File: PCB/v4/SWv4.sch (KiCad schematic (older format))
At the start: 5 parts

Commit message: start v4 schem
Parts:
- added C? (x2): 1uF, symbol C
- added C?: 10uF/16V, symbol C
- added J?: LRA, symbol CONN_01X02
- added R?: 920K, symbol R
- added R? (x4): 10K, symbol R
- added SW?: BTN_TL, symbol SW_Push_45deg
- added SW?: BTN_BL, symbol SW_Push_45deg
- added SW?: BTN_BR, symbol SW_Push_45deg
- added SW?: BTN_TR, symbol SW_Push_45deg
- added U?: CP2102, symbol CP2102
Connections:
- net labels added: +12V, +3V3, +BATT, CS(OLED), D/C, GND, MOSI, RST(OLED), SCLK
- wire segments 0 -> 33
- no-connect marks 0 -> 1
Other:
- moved on the sheet: U?, X?

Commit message: update v4 schem & create v4 sheets
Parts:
- removed J?: Micro_SD_Card, symbol Micro_SD_Card
- removed R? (x3): 10K, symbol R
- removed SW?: BTN_BL, symbol SW_Push_45deg
- removed SW?: BTN_BR, symbol SW_Push_45deg
- removed SW?: BTN_TR, symbol SW_Push_45deg
- added C? (x3): 10uF, symbol C
- added C?: 0.1uF, symbol C
- added C?: 10uF/15V, symbol C
- added C?: 10uF/16V, symbol C
- added D?: BAT54T1G, symbol D_Schottky_Small
- added J?: Micro_SD_Card_SPI, symbol Micro_SD_Card_SPI
- added L?: 10uH, symbol L
- added R? (x4): 10K, symbol R
- added R?: 100K, symbol R
- added SW?: BTN_TR, symbol SW_Push_45deg
- added SW?: BTN_BL, symbol SW_Push_45deg
- added SW?: BTN_BR, symbol SW_Push_45deg
- added U?: FAN5331, symbol FAN5331
- J?: value USB_OTG -> microUSB
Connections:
- net labels added: +5V, BTN-BL, BTN-BR, BTN-TL, BTN-TR, CS(SD), D+, D-, MISO, RXD, SCL, SDA, TXD
- wire segments 33 -> 92
- no-connect marks 1 -> 17
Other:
- note added: "Buttons"
- note added: "Display Voltage Boost"
- note added: "Haptics"
- note added: "OLED Display\nInterface"
- note added: "SD Card (SPI) - SD Interface Compat. ?"
- note added: "USB interface (Serial / PWR)"
- moved on the sheet: C?, J?, R?, SW?, U?

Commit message: sync
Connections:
- net DRV_EN: now reaches U?.5 (EN)
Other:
- moved on the sheet: C?

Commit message: sync
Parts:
- removed R? (x4): 10K, symbol R
- removed SW?: BTN_TL, symbol SW_Push_45deg
- removed SW?: BTN_TR, symbol SW_Push_45deg
- removed SW?: BTN_BL, symbol SW_Push_45deg
- removed SW?: BTN_BR, symbol SW_Push_45deg
- added C? (x4): 1nF/50V, symbol C
- added Q? (x2): S8050(NPN), TO_SOT_Packages_THT:TO-92_Molded_Narrow, symbol S8050
- added R? (x4): 470R, symbol R
- added R? (x4): 5K, symbol R
- added R? (x2): 12K, symbol R
- added SW?: BTN_TL, symbol SW_Push_45deg
- added SW?: BTN_TR, symbol SW_Push_45deg
- added SW?: BTN_BL, symbol SW_Push_45deg
- added SW?: BTN_BR, symbol SW_Push_45deg
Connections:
- net +3V3: now also R?.1, R?.1, R?.1, R?.1
- net BTN-BL: now also R?.2, R?.2
- net BTN-BR: now also R?.2, R?.2
- net BTN-TL: now also R?.2, R?.2
- net BTN-TR: now also R?.2, R?.2
- net GND: now also U?.1 (GND), U?.15 (GND), U?.38 (GND), U?.39 (GND-PAD), C?.2, C?.2, C?.2, C?.2, SW?.2, SW?.2, SW?.2, SW?.2
- net RXD: no longer U?.25 (RXD)
- net TXD: no longer U?.26 (TXD)
- net IO0: now reaches U?.25 (IO0)
- net IO0: now also Q?.3 (C)
- net ESP_EN: now reaches U?.3 (EN)
- net ESP_EN: now also Q?.3 (C)
- net RTS: now reaches U?.24 (RTS)
- net RTS: now also Q?.1 (E), R?.2
- net DTR: now reaches U?.28 (DTR)
- net DTR: now also Q?.1 (E), R?.2
- new net: C?.1, R?.1, SW?.1 (x4)
- new net: Q?.2 (B), R?.1 (x2)
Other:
- note added: "Add BTN-?? here"
- note added: "Auto Reset"

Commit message: start adafruit rebase
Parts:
- removed U?: CP2102, symbol CP2102
- added C? (x4): 10uF, symbol C
- added C?: 1uF, symbol C
- added D?: LED, symbol LED
- added D?: D_Schottky, symbol D_Schottky
- added J?: BATT, symbol CONN_01X02
- added R?: 1K, symbol R
- added R?: ???K, symbol R
- added R? (x2): 100K, symbol R
- added U?: CP2104, symbol CP2104
- added U?: MCP73831/2, symbol MCP73831/2
- added U?: AP2112/3V3, symbol AP2112/3V3
- R? (x2): value 12K -> 10K
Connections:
- net +3V3: now also C?.1, C?.1, C?.1, U?.5 (OUT), U?.5 (VIO), U?.6 (VDD), U?.7 (REGIN)
- net +5V: now also D?.2 (A), D?.2 (A), R?.1, U?.4 (VDD), U?.8 (VBUS)
- net +BATT: now also C?.2, J?.1 (P1), U?.3 (VBAT)
- net D+: now also U?.3 (D+)
- net D-: now also U?.4 (D-)
- net DTR: now also U?.23 (DTR)
- net GND: now also C?.1, C?.2, C?.2, C?.2, C?.2, J?.2 (P2), R?.2, R?.2, U?.2 (GND), U?.2 (GND), U?.2 (VSS)
- net RTS: now also U?.19 (RTS)
- net RXD: now also U?.20 (RXD)
- net TXD: now also U?.21 (TXD)
- new net: D?.1 (K), R?.1
- new net: R?.2, U?.1 (STAT)
- new net: R?.1, U?.5 (PROG)
- new net: C?.1, D?.1 (K), R?.1, U?.1 (IN)
- new net: R?.2, U?.3 (EN)
- no-connect marks 17 -> 20
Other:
- note added: "LIPO Charge"
- note added: "Power / Filtering?"
- note added: "Ref Ada\n(Link GNDs?)"
- note added: "USB Interface"
- note removed: "USB interface (Serial / PWR)"
- moved on the sheet: Q?, R?

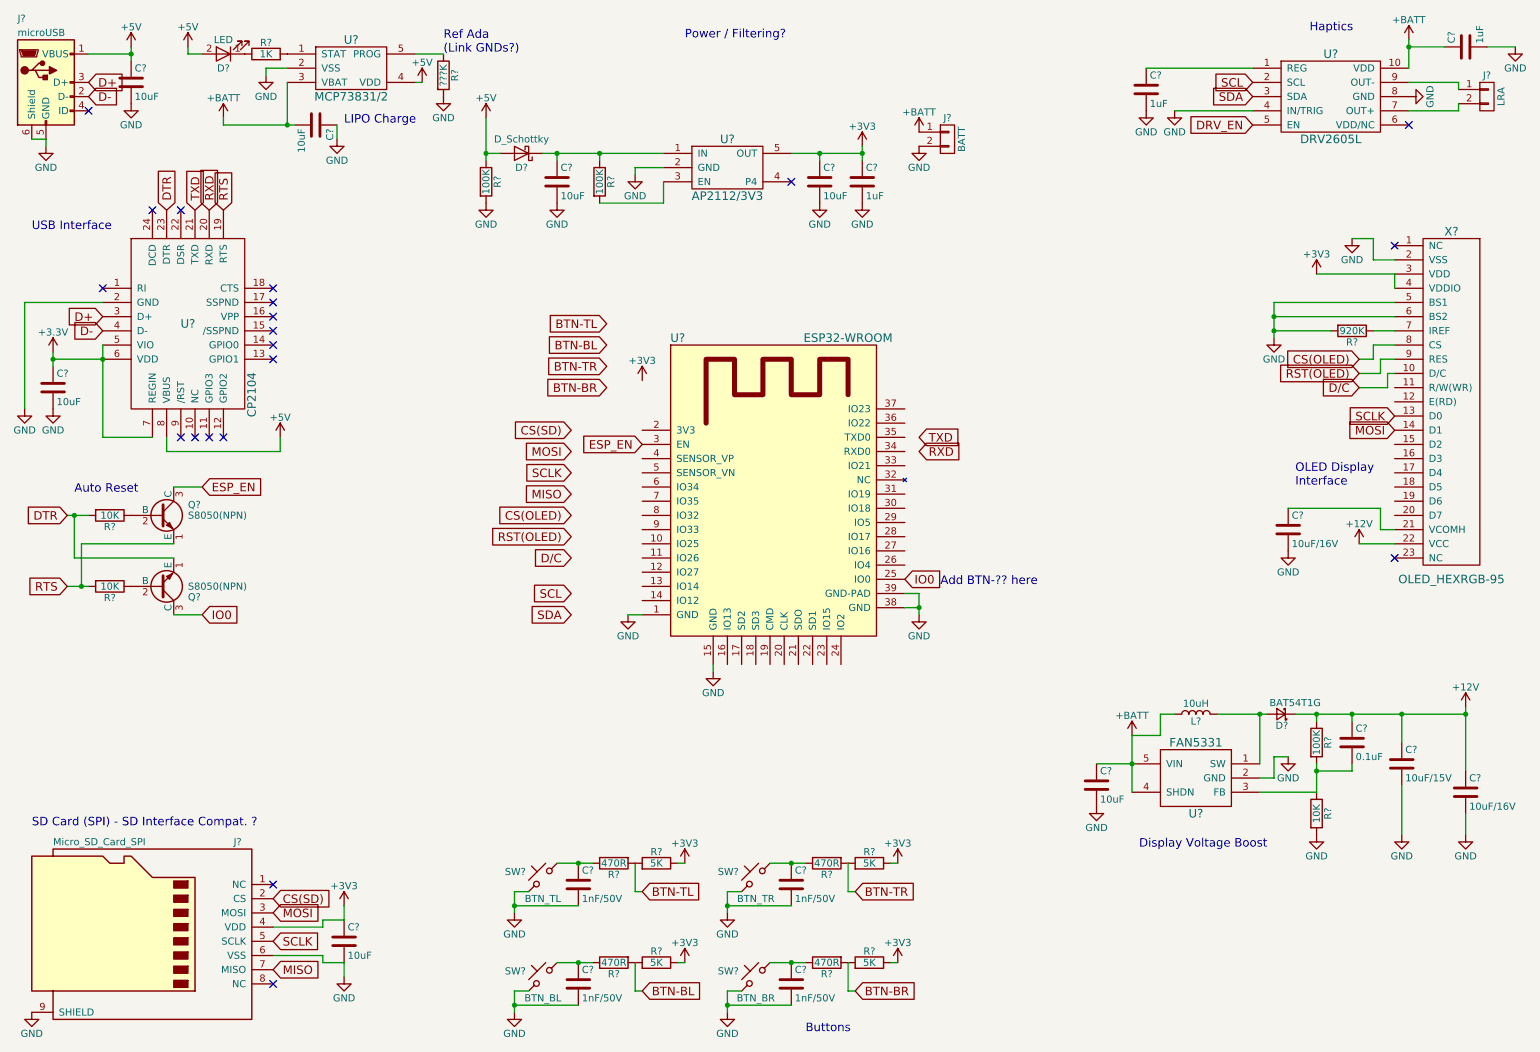
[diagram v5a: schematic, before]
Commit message: add feather ref & feather vbatt-lvl
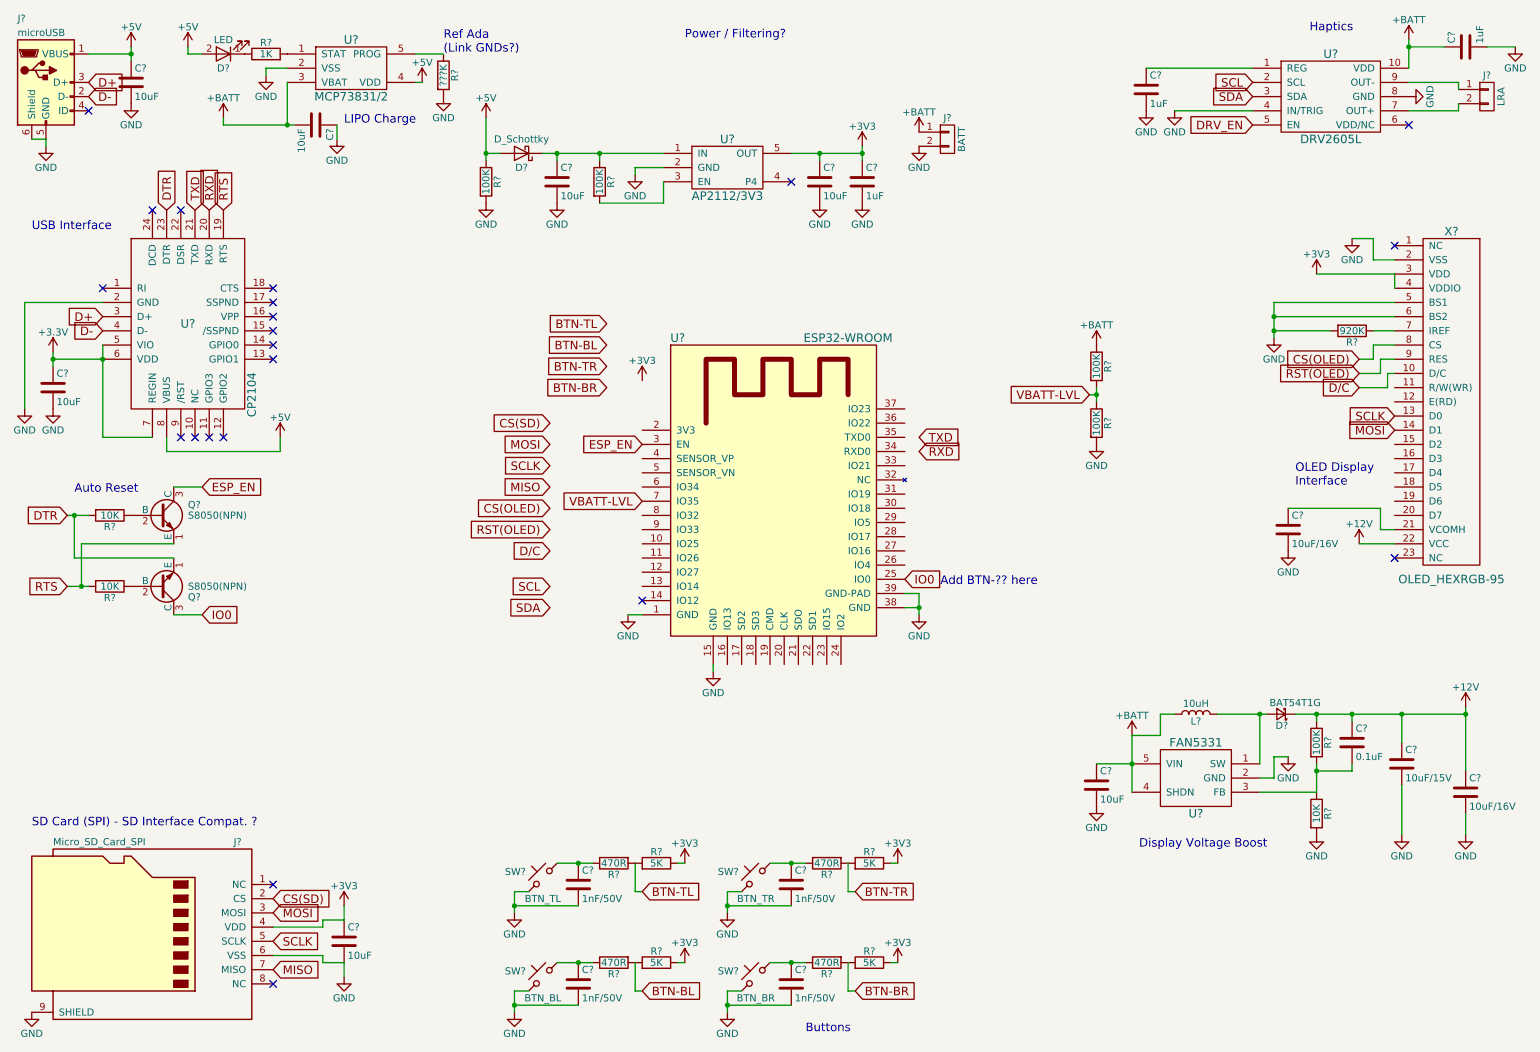
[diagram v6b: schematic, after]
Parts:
- added R? (x2): 100K, symbol R
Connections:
- net +BATT: now also R?.1
- net GND: now also R?.2
- net VBATT-LVL: now reaches U?.7 (IO35)
- net VBATT-LVL: now also R?.1, R?.2
- no-connect marks 20 -> 21
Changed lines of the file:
@@
 Text GLabel 4700 3150 0    60   Input ~ 0
 BTN-BR
-Text GLabel 4450 3450 0    60   Input ~ 0
+Text GLabel 4300 3400 0    60   Input ~ 0
 CS(SD)
-Text GLabel 4450 3600 0    60   Input ~ 0
+Text GLabel 4300 3550 0    60   Input ~ 0
 MOSI
-Text GLabel 4450 3750 0    60   Input ~ 0
+Text GLabel 4300 3700 0    60   Input ~ 0
 SCLK
-Text GLabel 4450 3900 0    60   Input ~ 0
+Text GLabel 4300 3850 0    60   Input ~ 0
 MISO
-Text GLabel 4450 4050 0    60   Input ~ 0
+Text GLabel 4300 4000 0    60   Input ~ 0
 CS(OLED)
-Text GLabel 4450 4200 0    60   Input ~ 0
+Text GLabel 4300 4150 0    60   Input ~ 0
 RST(OLED)
-Text GLabel 4450 4350 0    60   Input ~ 0
+Text GLabel 4300 4300 0    60   Input ~ 0
 D/C
-Text GLabel 4450 4600 0    60   Input ~ 0
+Text GLabel 4300 4550 0    60   Input ~ 0
 SCL
-Text GLabel 4450 4750 0    60   Input ~ 0
+Text GLabel 4300 4700 0    60   Input ~ 0
 SDA
 Text GLabel 1800 1900 1    60   Input ~ 0
@@
 	10700 1200 10700 1150
 Wire Wire Line
-	10350 700  10350 750
-Wire Wire Line
-	10350 750  10350 900
+	10350 700  10350 900
 Connection ~ 10350 750
 Wire Wire Line
@@
 	10250 2650 9400 2650
 Wire Wire Line
-	9400 2550 9400 2650
-Wire Wire Line
-	9400 2650 9400 2750
-Wire Wire Line
-	9400 2750 9400 2800
+	9400 2550 9400 2800
 Wire Wire Line
 	10250 2550 9400 2550
@@
 	1050 800  1350 800
 Wire Wire Line
-	1350 750  1350 800
-Wire Wire Line
-	1350 800  1350 850
+	1350 750  1350 850
 Connection ~ 1350 800
 Wire Wire Line
-	8400 5600 8400 5800
-Wire Wire Line
-	8400 5800 8400 6000
+	8400 5600 8400 6000
 Connection ~ 8400 5800
 Wire Wire Line
@@
 	9300 5800 9300 5450
 Wire Wire Line
-	9000 5450 9300 5450
-Wire Wire Line
-	9300 5450 9350 5450
+	9000 5450 9350 5450
 Connection ~ 9300 5450
 Wire Wire Line
@@
 	9700 6000 9300 6000
 Wire Wire Line
-	9550 5450 9700 5450
-Wire Wire Line
-	9700 5450 9950 5450
-Wire Wire Line
-	9950 5450 10300 5450
-Wire Wire Line
-	10300 5450 10750 5450
+	9550 5450 10750 5450
 Wire Wire Line
 	10300 5450 10300 5650
@@
 	10750 6300 10750 6150
 Wire Wire Line
-	10750 5400 10750 5450
-Wire Wire Line
-	10750 5450 10750 5850
+	10750 5400 10750 5850
 Connection ~ 10750 5450
 Connection ~ 10300 5450
@@
 Connection ~ 9950 5450
 Wire Wire Line
-	9700 5800 9700 5850
-Wire Wire Line
-	9700 5850 9700 6000
+	9700 5800 9700 6000
 Wire Wire Line
 	9700 5850 9950 5850
@@
 	6800 4600 6900 4600
 Wire Wire Line
-	6900 4600 6900 4700
-Wire Wire Line
-	6900 4700 6900 4750
+	6900 4600 6900 4750
 Wire Wire Line
 	6800 4700 6900 4700
@@
 	1650 4750 1850 4750
 Wire Wire Line
-	900  4050 950  4050
-Wire Wire Line
-	950  4050 1050 4050
-Wire Wire Line
-	900  4550 1000 4550
-Wire Wire Line
-	1000 4550 1050 4550
+	900  4050 1050 4050
+Wire Wire Line
+	900  4550 1050 4550
 Wire Wire Line
 	950  4350 1650 4350
@@
 	4050 6700 4150 6700
 Wire Wire Line
-	4050 6700 4050 6800
-Wire Wire Line
-	4050 6800 4050 6850
+	4050 6700 4050 6850
 Wire Wire Line
 	4050 6800 4500 6800
 Connection ~ 4050 6800
 Wire Wire Line
-	4350 6500 4500 6500
-Wire Wire Line
-	4500 6500 4600 6500
+	4350 6500 4600 6500
 Connection ~ 4500 6500
 Wire Wire Line
@@
 	5550 6700 5650 6700
 Wire Wire Line
-	5550 6700 5550 6800
-Wire Wire Line
-	5550 6800 5550 6850
+	5550 6700 5550 6850
 Wire Wire Line
 	5550 6800 6000 6800
 Connection ~ 5550 6800
 Wire Wire Line
-	5850 6500 6000 6500
-Wire Wire Line
-	6000 6500 6100 6500
+	5850 6500 6100 6500
 Connection ~ 6000 6500
 Wire Wire Line
@@
 	4050 7400 4150 7400
 Wire Wire Line
-	4050 7400 4050 7500
-Wire Wire Line
-	4050 7500 4050 7550
+	4050 7400 4050 7550
 Wire Wire Line
 	4050 7500 4500 7500
 Connection ~ 4050 7500
 Wire Wire Line
-	4350 7200 4500 7200
-Wire Wire Line
-	4500 7200 4600 7200
+	4350 7200 4600 7200
 Connection ~ 4500 7200
 Wire Wire Line
@@
 	5550 7400 5650 7400
 Wire Wire Line
-	5550 7400 5550 7500
-Wire Wire Line
-	5550 7500 5550 7550
+	5550 7400 5550 7550
 Wire Wire Line
 	5550 7500 6000 7500
 Connection ~ 5550 7500
 Wire Wire Line
-	5850 7200 6000 7200
-Wire Wire Line
-	6000 7200 6100 7200
+	5850 7200 6100 7200
 Connection ~ 6000 7200
 Wire Wire Line
@@
 	2400 3600 2400 3500
 Wire Wire Line
-	1150 2850 1150 2950
-Wire Wire Line
-	1150 2950 1150 3500
+	1150 2850 1150 3500
 Wire Wire Line
 	1150 3500 1500 3500
 Connection ~ 1150 2950
 Wire Wire Line
-	800  2900 800  2950
-Wire Wire Line
-	800  2950 800  3000
+	800  2900 800  3000
 Wire Wire Line
 	800  2950 1150 2950
@@
 	2450 1000 2450 1300
 Wire Wire Line
-	2000 1300 2450 1300
-Wire Wire Line
-	2450 1300 2500 1300
+	2000 1300 2500 1300
 Wire Wire Line
 	2300 950  2300 900
@@
 	2000 1250 2000 1300
 Wire Wire Line
-	6000 1500 6200 1500
-Wire Wire Line
-	6200 1500 6500 1500
+	6000 1500 6500 1500
 Wire Wire Line
 	6200 1500 6200 1550
 Wire Wire Line
-	6500 1450 6500 1500
-Wire Wire Line
-	6500 1500 6500 1550
+	6500 1450 6500 1550
 Connection ~ 6200 1500
 Connection ~ 6500 1500
 Wire Wire Line
-	4250 1500 4350 1500
-Wire Wire Line
-	4350 1500 4650 1500
-Wire Wire Line
-	4650 1500 5100 1500
+	4250 1500 5100 1500
 Wire Wire Line
 	5100 1700 5100 1850
@@
 	3850 1500 3950 1500
 Wire Wire Line
-	3850 1250 3850 1500
-Wire Wire Line
-	3850 1500 3850 1550
+	3850 1250 3850 1550
 $Comp
 L +5V #PWR?
@@
 $EndComp
 Connection ~ 3850 1500
+NoConn ~ 4950 4650
+$Comp
+L R R?
+U 1 1 5924E8FD
+P 8150 3000
+F 0 "R?" V 8230 3000 50  0000 C CNN
+F 1 "100K" V 8150 3000 50  0000 C CNN
+F 2 "" V 8080 3000 50  0001 C CNN
+F 3 "" H 8150 3000 50  0001 C CNN
+	1    8150 3000
+	1    0    0    -1
+$EndComp
+$Comp
+L R R?
+U 1 1 5924EA32
+P 8150 3400
+F 0 "R?" V 8230 3400 50  0000 C CNN
+F 1 "100K" V 8150 3400 50  0000 C CNN
+F 2 "" V 8080 3400 50  0001 C CNN
+F 3 "" H 8150 3400 50  0001 C CNN
+	1    8150 3400
+	1    0    0    -1
+$EndComp
+$Comp
+L GND #PWR?
+U 1 1 5924EADE
+P 8150 3550
+F 0 "#PWR?" H 8150 3300 50  0001 C CNN
+F 1 "GND" H 8150 3400 50  0000 C CNN
+F 2 "" H 8150 3550 50  0001 C CNN
+F 3 "" H 8150 3550 50  0001 C CNN
+	1    8150 3550
+	1    0    0    -1
+$EndComp
+$Comp
+L +BATT #PWR?
+U 1 1 5924EB66
+P 8150 2850
+F 0 "#PWR?" H 8150 2700 50  0001 C CNN
+F 1 "+BATT" H 8150 2990 50  0000 C CNN
+F 2 "" H 8150 2850 50  0001 C CNN
+F 3 "" H 8150 2850 50  0001 C CNN
+	1    8150 2850
+	1    0    0    -1
+$EndComp
+Wire Wire Line
+	8150 3150 8150 3250
+Text GLabel 8100 3200 0    60   Input ~ 0
+VBATT-LVL
+Connection ~ 8150 3200
+Wire Wire Line
+	8100 3200 8150 3200
+Text GLabel 4950 3950 0    60   Input ~ 0
+VBATT-LVL
 $EndSCHEMATC
